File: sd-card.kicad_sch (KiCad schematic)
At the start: 2 parts, among them J7 Micro-SD-card

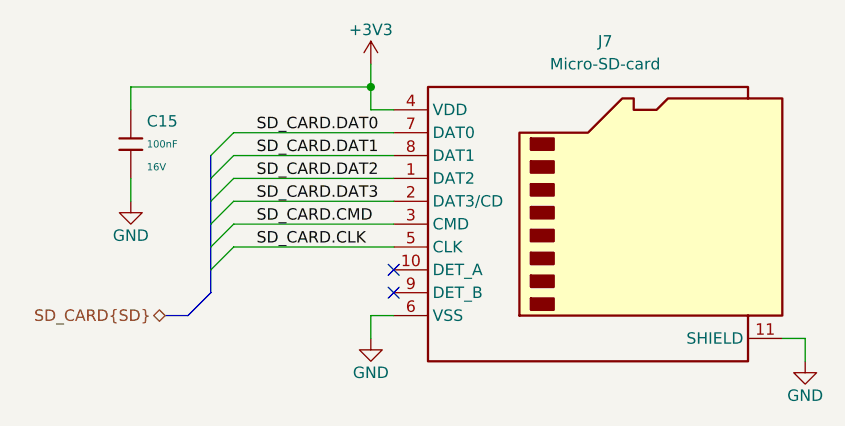
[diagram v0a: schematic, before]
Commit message: [#1] WIP: Change components to ones from the global library, refactor schematic
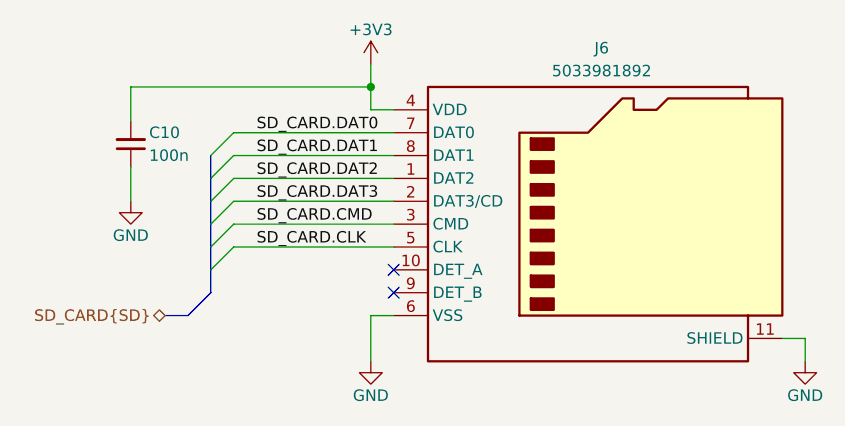
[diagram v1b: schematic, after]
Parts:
- removed C15: 100nF, PCM_JLCPCB:C_0402, symbol PCM_JLCPCB-Capacitors:0402,100nF
- added C10: C-100n-0402, DW-footprints:C_0402_1005Metric, symbol DW-capacitors:C-100n-0402
- J6: renamed from J7; value Micro-SD-card -> MicroSD_5033981892; footprint lib:mirco-SD-card-connector-503398-1892 -> DW-footprints:MicroSD_5033981892; symbol connectors:mirco-SD-card-connector-503398-1892 -> DW-connectors:MicroSD_5033981892; LCSC (none) -> C428492; MPN 503398-1892 -> 5033981892; Manufacturer (none) -> MOLEX
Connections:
- net +3V3: now also C10.2
- net GND: now also C10.1

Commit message: [#1] Re-annotate schematic
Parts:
- renumbered C10 to C24, J6 to J10
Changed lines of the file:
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@@
 		(on_board yes)
 		(dnp no)
-		(property "Reference" "C10"
+		(property "Reference" "C24"
 			(at 144.272 118.11 90)
 			(effects
@@
 			(project ""
 				(path "/090a8e41-87a8-4fb1-998b-60a2c0dc4cee/df5d742e-fec8-4307-bd86-008404d5e8ea"
-					(reference "C10")
+					(reference "C24")
 					(unit 1)
 				)
@@
 		(on_board yes)
 		(dnp no)
-		(property "Reference" "#PWR52"
+		(property "Reference" "#PWR078"
 			(at 217.17 149.86 0)
 			(effects
@@
 			(project "cm5-module"
 				(path "/090a8e41-87a8-4fb1-998b-60a2c0dc4cee/df5d742e-fec8-4307-bd86-008404d5e8ea"
-					(reference "#PWR52")
+					(reference "#PWR078")
 					(unit 1)
 				)
@@
 		(on_board yes)
 		(dnp no)
-		(property "Reference" "#PWR51"
+		(property "Reference" "#PWR077"
 			(at 168.91 149.86 0)
 			(effects
@@
 			(project "cm5-module"
 				(path "/090a8e41-87a8-4fb1-998b-60a2c0dc4cee/df5d742e-fec8-4307-bd86-008404d5e8ea"
-					(reference "#PWR51")
+					(reference "#PWR077")
 					(unit 1)
 				)
@@
 		(on_board yes)
 		(dnp no)
-		(property "Reference" "J6"
+		(property "Reference" "J10"
 			(at 194.564 108.712 0)
 			(effects
@@
 			(project ""
 				(path "/090a8e41-87a8-4fb1-998b-60a2c0dc4cee/df5d742e-fec8-4307-bd86-008404d5e8ea"
-					(reference "J6")
+					(reference "J10")
 					(unit 1)
 				)
@@
 		(on_board yes)
 		(dnp no)
-		(property "Reference" "#PWR015"
+		(property "Reference" "#PWR075"
 			(at 168.91 114.3 0)
 			(effects
@@
 			(project "cm5-module"
 				(path "/090a8e41-87a8-4fb1-998b-60a2c0dc4cee/df5d742e-fec8-4307-bd86-008404d5e8ea"
-					(reference "#PWR015")
+					(reference "#PWR075")
 					(unit 1)
 				)
@@
 		(on_board yes)
 		(dnp no)
-		(property "Reference" "#PWR50"
+		(property "Reference" "#PWR076"
 			(at 142.24 132.08 0)
 			(effects
@@
 			(project "cm5-module"
 				(path "/090a8e41-87a8-4fb1-998b-60a2c0dc4cee/df5d742e-fec8-4307-bd86-008404d5e8ea"
-					(reference "#PWR50")
+					(reference "#PWR076")
 					(unit 1)
 				)

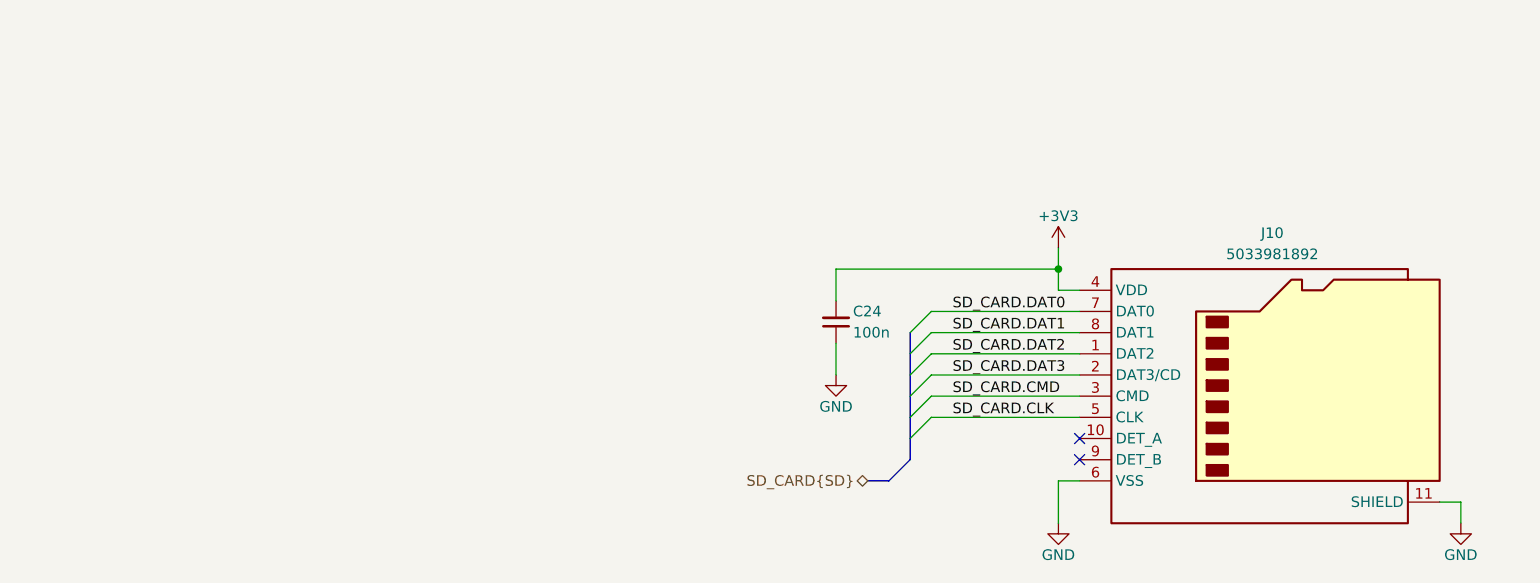
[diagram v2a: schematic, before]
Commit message: [#1] WIP: Refactor schematic
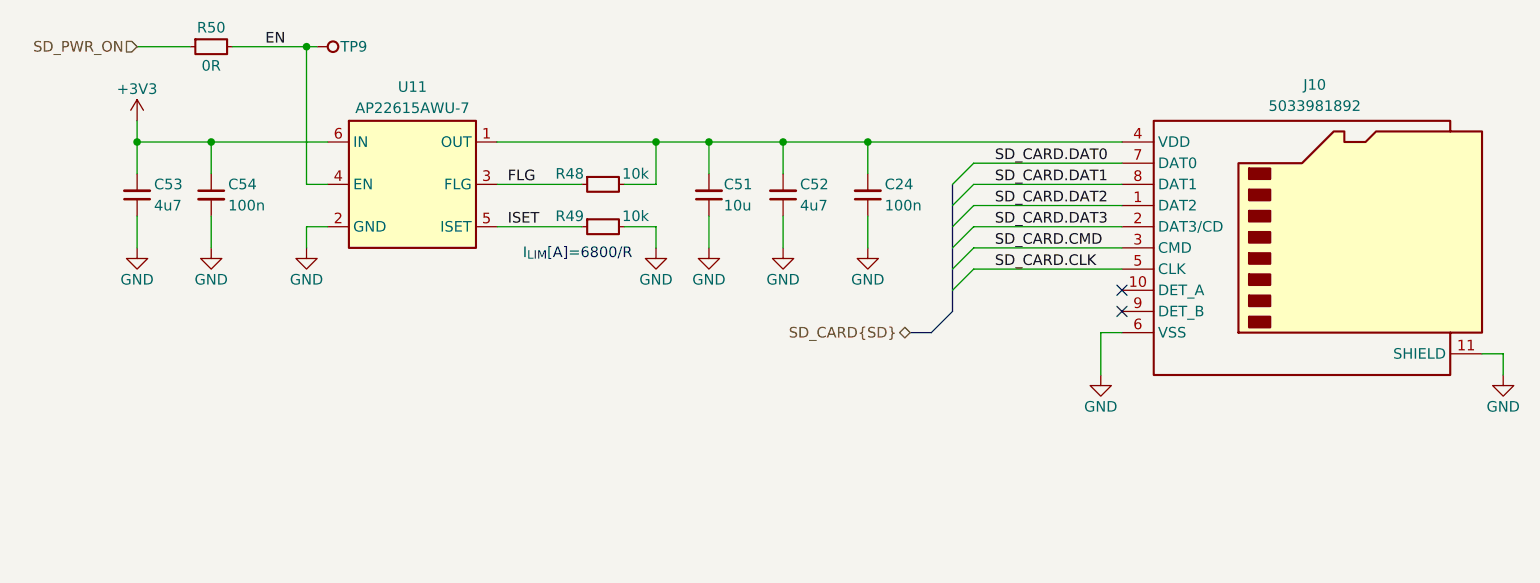
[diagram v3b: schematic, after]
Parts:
- added C51: C-10u-0603, DW-footprints:C_0603_1608Metric, symbol DW-capacitors:C-10u-0603
- added C52, C53: C-4u7-0402, DW-footprints:C_0402_1005Metric, symbol DW-capacitors:C-4u7-0402
- added C54: C-100n-0402, DW-footprints:C_0402_1005Metric, symbol DW-capacitors:C-100n-0402
- added R48, R49: R-10k-0402, DW-footprints:R_0402_1005Metric, symbol DW-resistors:R-10k-0402
- added R50: R-0R-0402, DW-footprints:R_0402_1005Metric, symbol DW-resistors:R-0R-0402
- added TP9: TP_SMD_0.75mm, DW-footprints:TP_SMD_0.75mm, symbol DW-test-points:TP_SMD_0.75mm
- added U11: AP22615AWU-7, DW-footprints:TSOT-23-6, symbol DW-ICs:AP22615AWU-7
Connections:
- net +3V3: now also C53.2, C54.1, U11.6 (IN); no longer C24.2, J10.4 (VDD)
- net GND: now also C51.1, C52.1, C53.1, C54.2, R49.2, U11.2 (GND)
- new net: C24.2, C51.2, C52.2, J10.4 (VDD), R48.2, U11.1 (OUT)
- new net EN: R50.2, TP9.1, U11.4 (EN)
- new net FLG: R48.1, U11.3 (FLG)
- new net ISET: R49.1, U11.5 (ISET)
- new net SD_PWR_ON: R50.1
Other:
- note added: "I_{LIM}[A]=6800/R"
- moved on the sheet: C24, J10

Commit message: [#3] Continue layout, minor schematic fixes, add power switch for CAN transceiver 5V rail
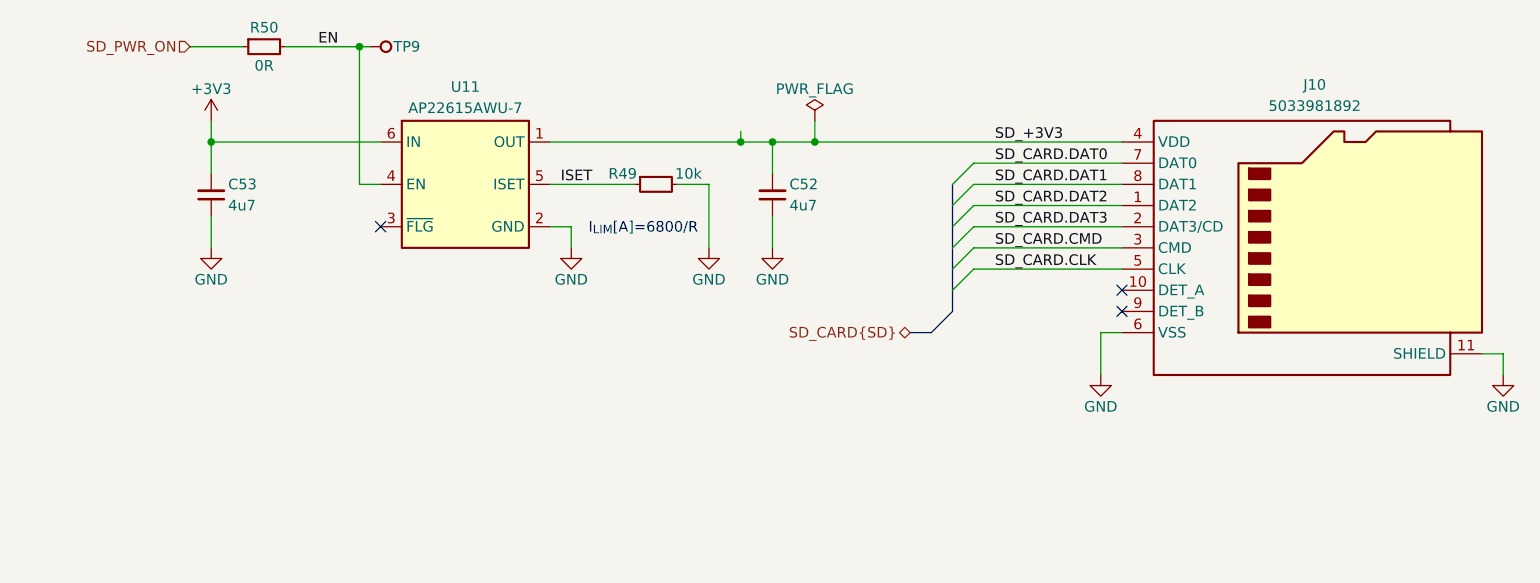
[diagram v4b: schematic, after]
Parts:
- removed C24, C54: C-100n-0402, DW-footprints:C_0402_1005Metric, symbol DW-capacitors:C-100n-0402
- removed C51: C-10u-0603, DW-footprints:C_0603_1608Metric, symbol DW-capacitors:C-10u-0603
- removed R48: R-10k-0402, DW-footprints:R_0402_1005Metric, symbol DW-resistors:R-10k-0402
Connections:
- net SD_+3V3: now reaches C52.2, J10.4 (VDD), U11.1 (OUT)
- net FLG: no longer names the net of U11.3 (~{FLG})
- no-connect marks 2 -> 3
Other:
- moved on the sheet: C52, C53, R49, R50, TP9, U11

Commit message: [#3] WIP: Clear ERC, re-annotate schematic
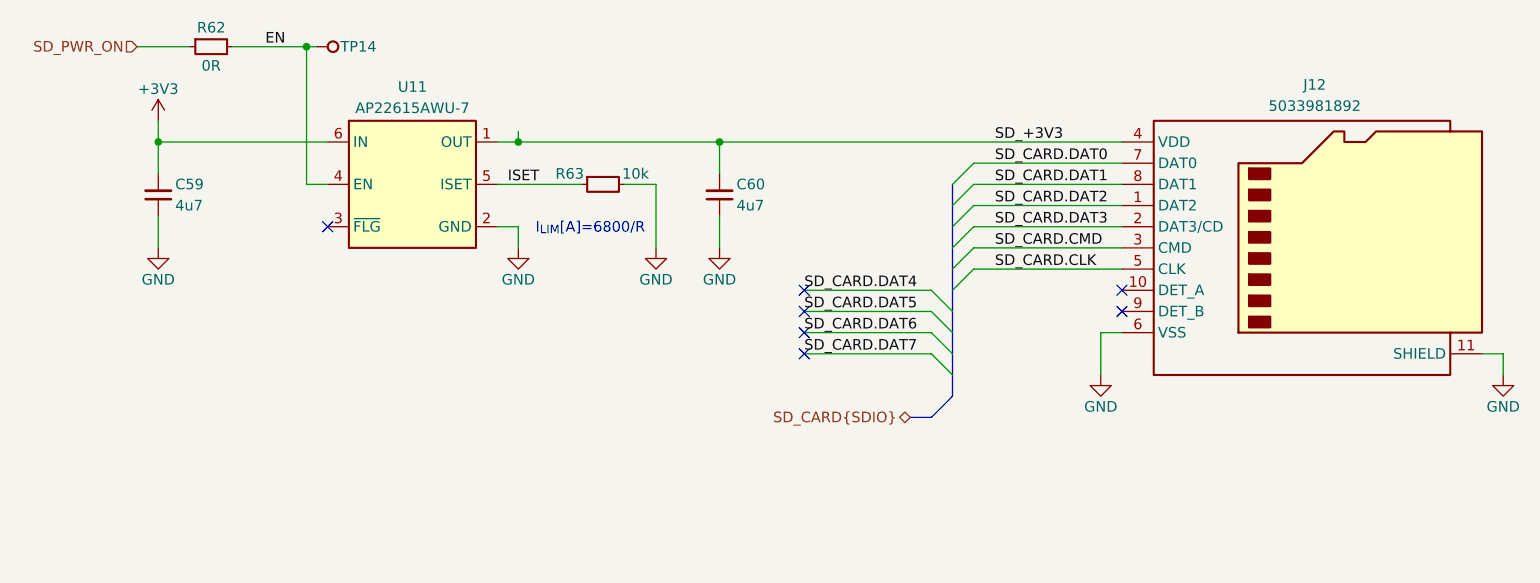
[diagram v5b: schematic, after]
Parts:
- renumbered C53 to C59, C52 to C60, J10 to J12, R50 to R62, R49 to R63, TP9 to TP14
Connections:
- no-connect marks 3 -> 7
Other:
- moved on the sheet: C59, C60, R62, R63, TP14, U11

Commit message: [#3] Re-annotate schematic
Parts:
- renumbered C59 to C39, C60 to C40, J12 to J7, R62 to R36, R63 to R37, TP14 to TP8, U11 to U7
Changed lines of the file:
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@@
 		(on_board yes)
 		(dnp no)
-		(property "Reference" "C60"
+		(property "Reference" "C40"
 			(at 130.302 102.87 90)
 			(effects
@@
 			(project "cm5-module"
 				(path "/090a8e41-87a8-4fb1-998b-60a2c0dc4cee/df5d742e-fec8-4307-bd86-008404d5e8ea"
-					(reference "C60")
+					(reference "C40")
 					(unit 1)
 				)
@@
 		(on_board yes)
 		(dnp no)
-		(property "Reference" "#PWR0145"
+		(property "Reference" "#PWR088"
 			(at 60.96 116.84 0)
 			(effects
@@
 			(project "cm5-module"
 				(path "/090a8e41-87a8-4fb1-998b-60a2c0dc4cee/df5d742e-fec8-4307-bd86-008404d5e8ea"
-					(reference "#PWR0145")
+					(reference "#PWR088")
 					(unit 1)
 				)
@@
 		(on_board yes)
 		(dnp no)
-		(property "Reference" "#PWR0150"
+		(property "Reference" "#PWR093"
 			(at 222.25 132.08 0)
 			(effects
@@
 			(project "cm5-module"
 				(path "/090a8e41-87a8-4fb1-998b-60a2c0dc4cee/df5d742e-fec8-4307-bd86-008404d5e8ea"
-					(reference "#PWR0150")
+					(reference "#PWR093")
 					(unit 1)
 				)
@@
 		(on_board yes)
 		(dnp no)
-		(property "Reference" "#PWR0148"
+		(property "Reference" "#PWR091"
 			(at 128.27 116.84 0)
 			(effects
@@
 			(project "cm5-module"
 				(path "/090a8e41-87a8-4fb1-998b-60a2c0dc4cee/df5d742e-fec8-4307-bd86-008404d5e8ea"
-					(reference "#PWR0148")
+					(reference "#PWR091")
 					(unit 1)
 				)
@@
 		(on_board yes)
 		(dnp no)
-		(property "Reference" "#PWR0144"
+		(property "Reference" "#PWR087"
 			(at 60.96 99.06 0)
 			(effects
@@
 			(project "cm5-module"
 				(path "/090a8e41-87a8-4fb1-998b-60a2c0dc4cee/df5d742e-fec8-4307-bd86-008404d5e8ea"
-					(reference "#PWR0144")
+					(reference "#PWR087")
 					(unit 1)
 				)
@@
 		(on_board yes)
 		(dnp no)
-		(property "Reference" "#PWR0149"
+		(property "Reference" "#PWR092"
 			(at 173.99 132.08 0)
 			(effects
@@
 			(project "cm5-module"
 				(path "/090a8e41-87a8-4fb1-998b-60a2c0dc4cee/df5d742e-fec8-4307-bd86-008404d5e8ea"
-					(reference "#PWR0149")
+					(reference "#PWR092")
 					(unit 1)
 				)
@@
 		(on_board yes)
 		(dnp no)
-		(property "Reference" "J12"
+		(property "Reference" "J7"
 			(at 199.644 90.932 0)
 			(effects
@@
 			(project ""
 				(path "/090a8e41-87a8-4fb1-998b-60a2c0dc4cee/df5d742e-fec8-4307-bd86-008404d5e8ea"
-					(reference "J12")
+					(reference "J7")
 					(unit 1)
 				)
@@
 		(on_board yes)
 		(dnp no)
-		(property "Reference" "#PWR0146"
+		(property "Reference" "#PWR089"
 			(at 104.14 116.84 0)
 			(effects
@@
 			(project "cm5-module"
 				(path "/090a8e41-87a8-4fb1-998b-60a2c0dc4cee/df5d742e-fec8-4307-bd86-008404d5e8ea"
-					(reference "#PWR0146")
+					(reference "#PWR089")
 					(unit 1)
 				)
@@
 		(on_board yes)
 		(dnp no)
-		(property "Reference" "#PWR0147"
+		(property "Reference" "#PWR090"
 			(at 120.65 116.84 0)
 			(effects
@@
 			(project "cm5-module"
 				(path "/090a8e41-87a8-4fb1-998b-60a2c0dc4cee/df5d742e-fec8-4307-bd86-008404d5e8ea"
-					(reference "#PWR0147")
+					(reference "#PWR090")
 					(unit 1)
 				)
@@
 		(on_board yes)
 		(dnp no)
-		(property "Reference" "C59"
+		(property "Reference" "C39"
 			(at 62.992 102.87 90)
 			(effects
@@
 			(project "cm5-module"
 				(path "/090a8e41-87a8-4fb1-998b-60a2c0dc4cee/df5d742e-fec8-4307-bd86-008404d5e8ea"
-					(reference "C59")
+					(reference "C39")
 					(unit 1)
 				)
@@
 		(on_board yes)
 		(dnp no)
-		(property "Reference" "R62"
+		(property "Reference" "R36"
 			(at 67.31 84.074 0)
 			(effects
@@
 			(project "cm5-module"
 				(path "/090a8e41-87a8-4fb1-998b-60a2c0dc4cee/df5d742e-fec8-4307-bd86-008404d5e8ea"
-					(reference "R62")
+					(reference "R36")
 					(unit 1)
 				)
@@
 		(on_board yes)
 		(dnp no)
-		(property "Reference" "TP14"
+		(property "Reference" "TP8"
 			(at 82.804 86.36 0)
 			(effects
@@
 			(project "cm5-module"
 				(path "/090a8e41-87a8-4fb1-998b-60a2c0dc4cee/df5d742e-fec8-4307-bd86-008404d5e8ea"
-					(reference "TP14")
+					(reference "TP8")
 					(unit 1)
 				)
@@
 		(on_board yes)
 		(dnp no)
-		(property "Reference" "U11"
+		(property "Reference" "U7"
 			(at 91.44 91.186 0)
 			(effects
@@
 			(project "cm5-module"
 				(path "/090a8e41-87a8-4fb1-998b-60a2c0dc4cee/df5d742e-fec8-4307-bd86-008404d5e8ea"
-					(reference "U11")
+					(reference "U7")
 					(unit 1)
 				)
@@
 		(on_board yes)
 		(dnp no)
-		(property "Reference" "R63"
+		(property "Reference" "R37"
 			(at 112.014 101.6 0)
 			(effects
@@
 			(project "cm5-module"
 				(path "/090a8e41-87a8-4fb1-998b-60a2c0dc4cee/df5d742e-fec8-4307-bd86-008404d5e8ea"
-					(reference "R63")
-					(unit 1)
-				)
+					(reference "R37")
+					(unit 1)
+				)
